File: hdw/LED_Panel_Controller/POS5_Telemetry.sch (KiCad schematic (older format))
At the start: 7 parts

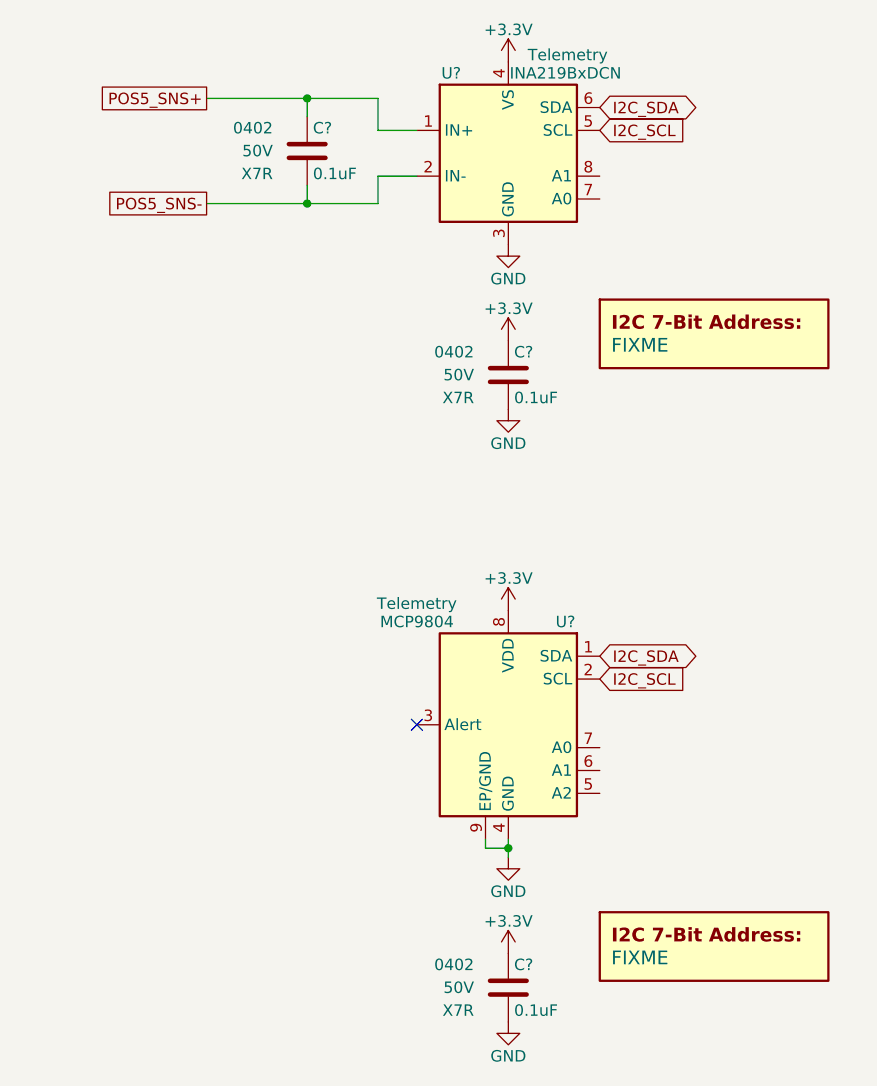
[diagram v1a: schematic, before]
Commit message: fixed level shifter sheet
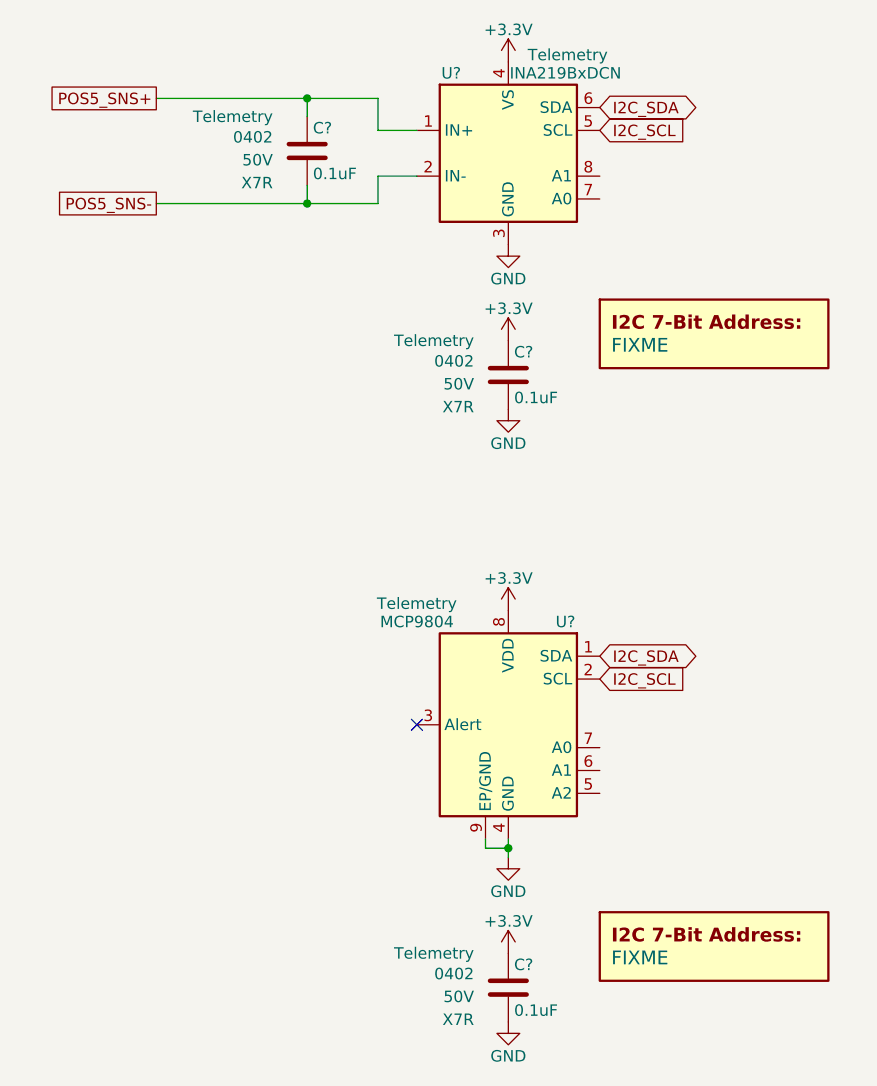
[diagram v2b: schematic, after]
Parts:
- removed C? (x3): 0.1uF, Capacitors_SMD:C_0402, symbol Custom_Library:C_Custom
- added C? (x3): 0.1uF, Capacitors_SMD:C_0402, symbol Custom_Library:C_Custom
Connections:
- net +3V3: now also C?.1, C?.1
- net GND: now also C?.2, C?.2
- net POS5_SNS+: now also C?.1
- net POS5_SNS-: now also C?.2
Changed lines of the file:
@@
 Comment4 ""
 $EndDescr
-Text GLabel 3790 1800 0    50   UnSpc ~ 0
+Text GLabel 3570 1800 0    50   UnSpc ~ 0
 POS5_SNS+
-Text GLabel 3790 2260 0    50   UnSpc ~ 0
+Text GLabel 3570 2260 0    50   UnSpc ~ 0
 POS5_SNS-
 $Comp
@@
 AR Path="/5EAE2D84/5E0ACFF2" Ref="#PWR?"  Part="1"
 AR Path="/5F581B58/5E0ACFF2" Ref="#PWR?"  Part="1"
+AR Path="/5F581B77/5E0ACFF2" Ref="#PWR?"  Part="1"
 AR Path="/5F581BB7/5E0ACFF2" Ref="#PWR?"  Part="1"
 F 0 "#PWR?" H 5110 2190 50  0001 C CNN
@@
 AR Path="/5EAE2D84/5E0AD665" Ref="#PWR?"  Part="1"
 AR Path="/5F581B58/5E0AD665" Ref="#PWR?"  Part="1"
+AR Path="/5F581B77/5E0AD665" Ref="#PWR?"  Part="1"
 AR Path="/5F581BB7/5E0AD665" Ref="#PWR?"  Part="1"
 F 0 "#PWR?" H 5110 1490 50  0001 C CNN
@@
 Text GLabel 5510 1940 2    50   Input ~ 0
 I2C_SCL
-$Comp
-L Custom_Library:C_Custom C?
-U 1 1 5E0B2427
-P 5110 3010
-AR Path="/5B3E071A/5E0B2427" Ref="C?"  Part="1"
-AR Path="/5E0652BA/5E0B2427" Ref="C?"  Part="1"
-AR Path="/5E0A0E29/5E0B2427" Ref="C?"  Part="1"
-AR Path="/5E052856/5E0B2427" Ref="C?"  Part="1"
-AR Path="/5EAE2D84/5E0B2427" Ref="C?"  Part="1"
-AR Path="/5F581B58/5E0B2427" Ref="C?"  Part="1"
-AR Path="/5F581BB7/5E0B2427" Ref="C?"  Part="1"
-F 0 "C?" H 5135 3110 50  0000 L CNN
-F 1 "0.1uF" H 5135 2910 50  0000 L CNN
-F 2 "Capacitors_SMD:C_0402" H 5148 2860 50  0001 C CNN
-F 3 "" H 5135 3110 50  0001 C CNN
-F 4 "0402" H 4960 3110 50  0000 R CNN "display_footprint"
-F 5 "50V" H 4960 3010 50  0000 R CNN "Voltage"
-F 6 "X7R" H 4960 2910 50  0000 R CNN "Dielectric"
-F 7 "" H 1200 -3870 50  0001 C CNN "Digi-Key PN"
-	1    5110 3010
-	1    0    0    -1
-$EndComp
 $Comp
 L power:+3.3V #PWR?
@@
 AR Path="/5EAE2D84/5E0B535B" Ref="#PWR?"  Part="1"
 AR Path="/5F581B58/5E0B535B" Ref="#PWR?"  Part="1"
+AR Path="/5F581B77/5E0B535B" Ref="#PWR?"  Part="1"
 AR Path="/5F581BB7/5E0B535B" Ref="#PWR?"  Part="1"
 F 0 "#PWR?" H 5110 2710 50  0001 C CNN
@@
 AR Path="/5EAE2D84/5E0B592B" Ref="#PWR?"  Part="1"
 AR Path="/5F581B58/5E0B592B" Ref="#PWR?"  Part="1"
+AR Path="/5F581B77/5E0B592B" Ref="#PWR?"  Part="1"
 AR Path="/5F581BB7/5E0B592B" Ref="#PWR?"  Part="1"
 F 0 "#PWR?" H 5110 2910 50  0001 C CNN
@@
 AR Path="/5EAE2D84/5E0B8BC8" Ref="DOC?"  Part="1"
 AR Path="/5F581B58/5E0B8BC8" Ref="DOC?"  Part="1"
+AR Path="/5F581B77/5E0B8BC8" Ref="DOC?"  Part="1"
 AR Path="/5F581BB7/5E0B8BC8" Ref="DOC?"  Part="1"
 F 0 "DOC?" H 6010 3130 60  0001 C CNN
@@
 AR Path="/5EAE2D84/5E2AA995" Ref="#PWR?"  Part="1"
 AR Path="/5F581B58/5E2AA995" Ref="#PWR?"  Part="1"
+AR Path="/5F581B77/5E2AA995" Ref="#PWR?"  Part="1"
 AR Path="/5F581BB7/5E2AA995" Ref="#PWR?"  Part="1"
 F 0 "#PWR?" H 5110 4870 50  0001 C CNN
@@
 AR Path="/5EAE2D84/5E2AA99A" Ref="#PWR?"  Part="1"
 AR Path="/5F581B58/5E2AA99A" Ref="#PWR?"  Part="1"
+AR Path="/5F581B77/5E2AA99A" Ref="#PWR?"  Part="1"
 AR Path="/5F581BB7/5E2AA99A" Ref="#PWR?"  Part="1"
 F 0 "#PWR?" H 5110 3890 50  0001 C CNN
@@
 AR Path="/5EAE2D84/5E2AA99D" Ref="U?"  Part="1"
 AR Path="/5F581B58/5E2AA99D" Ref="U?"  Part="1"
+AR Path="/5F581B77/5E2AA99D" Ref="U?"  Part="1"
 AR Path="/5F581BB7/5E2AA99D" Ref="U?"  Part="1"
 F 0 "U?" H 4860 4990 50  0000 C CNN
@@
 NoConn ~ 4710 4540
 $Comp
-L Custom_Library:C_Custom C?
-U 1 1 5E2AA9A1
-P 5110 5690
-AR Path="/5B3E071A/5E2AA9A1" Ref="C?"  Part="1"
-AR Path="/5E0652BA/5E2AA9A1" Ref="C?"  Part="1"
-AR Path="/5E0A0E29/5E2AA9A1" Ref="C?"  Part="1"
-AR Path="/5E052856/5E2AA9A1" Ref="C?"  Part="1"
-AR Path="/5EAE2D84/5E2AA9A1" Ref="C?"  Part="1"
-AR Path="/5F581B58/5E2AA9A1" Ref="C?"  Part="1"
-AR Path="/5F581BB7/5E2AA9A1" Ref="C?"  Part="1"
-F 0 "C?" H 5135 5790 50  0000 L CNN
-F 1 "0.1uF" H 5135 5590 50  0000 L CNN
-F 2 "Capacitors_SMD:C_0402" H 5148 5540 50  0001 C CNN
-F 3 "" H 5135 5790 50  0001 C CNN
-F 4 "0402" H 4960 5790 50  0000 R CNN "display_footprint"
-F 5 "50V" H 4960 5690 50  0000 R CNN "Voltage"
-F 6 "X7R" H 4960 5590 50  0000 R CNN "Dielectric"
-F 7 "" H 1200 -1190 50  0001 C CNN "Digi-Key PN"
-	1    5110 5690
-	1    0    0    -1
-$EndComp
-$Comp
 L power:+3.3V #PWR?
 U 1 1 5E2AA9A6
@@
 AR Path="/5EAE2D84/5E2AA9A6" Ref="#PWR?"  Part="1"
 AR Path="/5F581B58/5E2AA9A6" Ref="#PWR?"  Part="1"
+AR Path="/5F581B77/5E2AA9A6" Ref="#PWR?"  Part="1"
 AR Path="/5F581BB7/5E2AA9A6" Ref="#PWR?"  Part="1"
 F 0 "#PWR?" H 5110 5390 50  0001 C CNN
@@
 AR Path="/5EAE2D84/5E2AA9AD" Ref="#PWR?"  Part="1"
 AR Path="/5F581B58/5E2AA9AD" Ref="#PWR?"  Part="1"
+AR Path="/5F581B77/5E2AA9AD" Ref="#PWR?"  Part="1"
 AR Path="/5F581BB7/5E2AA9AD" Ref="#PWR?"  Part="1"
 F 0 "#PWR?" H 5110 5590 50  0001 C CNN
@@
 AR Path="/5EAE2D84/5E2AA9AF" Ref="DOC?"  Part="1"
 AR Path="/5F581B58/5E2AA9AF" Ref="DOC?"  Part="1"
+AR Path="/5F581B77/5E2AA9AF" Ref="DOC?"  Part="1"
 AR Path="/5F581BB7/5E2AA9AF" Ref="DOC?"  Part="1"
 F 0 "DOC?" H 6010 5810 60  0001 C CNN
@@
 Wire Wire Line
 	4230 1880 4230 1800
-$Comp
-L Custom_Library:C_Custom C?
-U 1 1 5E07E0FD
-P 4230 2030
-AR Path="/5B3E071A/5E07E0FD" Ref="C?"  Part="1"
-AR Path="/5E0652BA/5E07E0FD" Ref="C?"  Part="1"
-AR Path="/5E0A0E29/5E07E0FD" Ref="C?"  Part="1"
-AR Path="/5E052856/5E07E0FD" Ref="C?"  Part="1"
-AR Path="/5EAE2D84/5E07E0FD" Ref="C?"  Part="1"
-AR Path="/5F581B58/5E07E0FD" Ref="C?"  Part="1"
-AR Path="/5F581BB7/5E07E0FD" Ref="C?"  Part="1"
-F 0 "C?" H 4255 2130 50  0000 L CNN
-F 1 "0.1uF" H 4255 1930 50  0000 L CNN
-F 2 "Capacitors_SMD:C_0402" H 4268 1880 50  0001 C CNN
-F 3 "" H 4255 2130 50  0001 C CNN
-F 4 "0402" H 4080 2130 50  0000 R CNN "display_footprint"
-F 5 "50V" H 4080 2030 50  0000 R CNN "Voltage"
-F 6 "X7R" H 4080 1930 50  0000 R CNN "Dielectric"
-F 7 "" H 320 -4850 50  0001 C CNN "Digi-Key PN"
-	1    4230 2030
-	1    0    0    -1
-$EndComp
-Wire Wire Line
-	3790 2260 4230 2260
-Wire Wire Line
-	3790 1800 4230 1800
 $Comp
 L Analog_ADC:INA219BxDCN U?
@@
 	4540 2260 4230 2260
 Connection ~ 4230 2260
+$Comp
+L Custom_Library:C_Custom C?
+U 1 1 6018BD18
+P 4230 2030
+AR Path="/5B3E071A/6018BD18" Ref="C?"  Part="1"
+AR Path="/5E0652BA/6018BD18" Ref="C?"  Part="1"
+AR Path="/5E0A0E29/6018BD18" Ref="C?"  Part="1"
+AR Path="/5E052856/6018BD18" Ref="C?"  Part="1"
+AR Path="/5EAE2D84/6018BD18" Ref="C?"  Part="1"
+AR Path="/5F581B58/6018BD18" Ref="C?"  Part="1"
+AR Path="/5F581B77/6018BD18" Ref="C?"  Part="1"
+AR Path="/5F581BB7/6018BD18" Ref="C?"  Part="1"
+F 0 "C?" H 4255 2130 50  0000 L CNN
+F 1 "0.1uF" H 4255 1930 50  0000 L CNN
+F 2 "Capacitors_SMD:C_0402" H 4268 1880 50  0001 C CNN
+F 3 "" H 4255 2130 50  0001 C CNN
+F 4 "0402" H 4080 2090 50  0000 R CNN "display_footprint"
+F 5 "50V" H 4080 1990 50  0000 R CNN "Voltage"
+F 6 "X7R" H 4080 1890 50  0000 R CNN "Dielectric"
+F 7 "Telemetry" H 4080 2180 50  0000 R CNN "Configuration"
+	1    4230 2030
+	1    0    0    -1
+$EndComp
+Wire Wire Line
+	3570 1800 4230 1800
+Wire Wire Line
+	3570 2260 4230 2260
+$Comp
+L Custom_Library:C_Custom C?
+U 1 1 6018C640
+P 5110 5690
+AR Path="/5B3E071A/6018C640" Ref="C?"  Part="1"
+AR Path="/5E0652BA/6018C640" Ref="C?"  Part="1"
+AR Path="/5E0A0E29/6018C640" Ref="C?"  Part="1"
+AR Path="/5E052856/6018C640" Ref="C?"  Part="1"
+AR Path="/5EAE2D84/6018C640" Ref="C?"  Part="1"
+AR Path="/5F581B58/6018C640" Ref="C?"  Part="1"
+AR Path="/5F581B77/6018C640" Ref="C?"  Part="1"
+AR Path="/5F581BB7/6018C640" Ref="C?"  Part="1"
+F 0 "C?" H 5135 5790 50  0000 L CNN
+F 1 "0.1uF" H 5135 5590 50  0000 L CNN
+F 2 "Capacitors_SMD:C_0402" H 5148 5540 50  0001 C CNN
+F 3 "" H 5135 5790 50  0001 C CNN
+F 4 "0402" H 4960 5750 50  0000 R CNN "display_footprint"
+F 5 "50V" H 4960 5650 50  0000 R CNN "Voltage"
+F 6 "X7R" H 4960 5550 50  0000 R CNN "Dielectric"
+F 7 "Telemetry" H 4960 5840 50  0000 R CNN "Configuration"
+	1    5110 5690
+	1    0    0    -1
+$EndComp
+$Comp
+L Custom_Library:C_Custom C?
+U 1 1 6018CFFA
+P 5110 3010
+AR Path="/5B3E071A/6018CFFA" Ref="C?"  Part="1"
+AR Path="/5E0652BA/6018CFFA" Ref="C?"  Part="1"
+AR Path="/5E0A0E29/6018CFFA" Ref="C?"  Part="1"
+AR Path="/5E052856/6018CFFA" Ref="C?"  Part="1"
+AR Path="/5EAE2D84/6018CFFA" Ref="C?"  Part="1"
+AR Path="/5F581B58/6018CFFA" Ref="C?"  Part="1"
+AR Path="/5F581B77/6018CFFA" Ref="C?"  Part="1"
+AR Path="/5F581BB7/6018CFFA" Ref="C?"  Part="1"
+F 0 "C?" H 5135 3110 50  0000 L CNN
+F 1 "0.1uF" H 5135 2910 50  0000 L CNN
+F 2 "Capacitors_SMD:C_0402" H 5148 2860 50  0001 C CNN
+F 3 "" H 5135 3110 50  0001 C CNN
+F 4 "0402" H 4960 3070 50  0000 R CNN "display_footprint"
+F 5 "50V" H 4960 2970 50  0000 R CNN "Voltage"
+F 6 "X7R" H 4960 2870 50  0000 R CNN "Dielectric"
+F 7 "Telemetry" H 4960 3160 50  0000 R CNN "Configuration"
+	1    5110 3010
+	1    0    0    -1
+$EndComp
 $EndSCHEMATC

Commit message: added digikey pns, footprints, bom scrubbed
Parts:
- C? (x3): Digi-Key PN (none) -> 490-10701-1-ND
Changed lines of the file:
@@
 F 6 "X7R" H 4080 1890 50  0000 R CNN "Dielectric"
 F 7 "Telemetry" H 4080 2180 50  0000 R CNN "Configuration"
+F 8 "490-10701-1-ND" H 4230 2030 50  0001 C CNN "Digi-Key PN"
 	1    4230 2030
 	1    0    0    -1
@@
 F 6 "X7R" H 4960 5550 50  0000 R CNN "Dielectric"
 F 7 "Telemetry" H 4960 5840 50  0000 R CNN "Configuration"
+F 8 "490-10701-1-ND" H 5110 5690 50  0001 C CNN "Digi-Key PN"
 	1    5110 5690
 	1    0    0    -1
@@
 F 6 "X7R" H 4960 2870 50  0000 R CNN "Dielectric"
 F 7 "Telemetry" H 4960 3160 50  0000 R CNN "Configuration"
+F 8 "490-10701-1-ND" H 5110 3010 50  0001 C CNN "Digi-Key PN"
 	1    5110 3010
 	1    0    0    -1

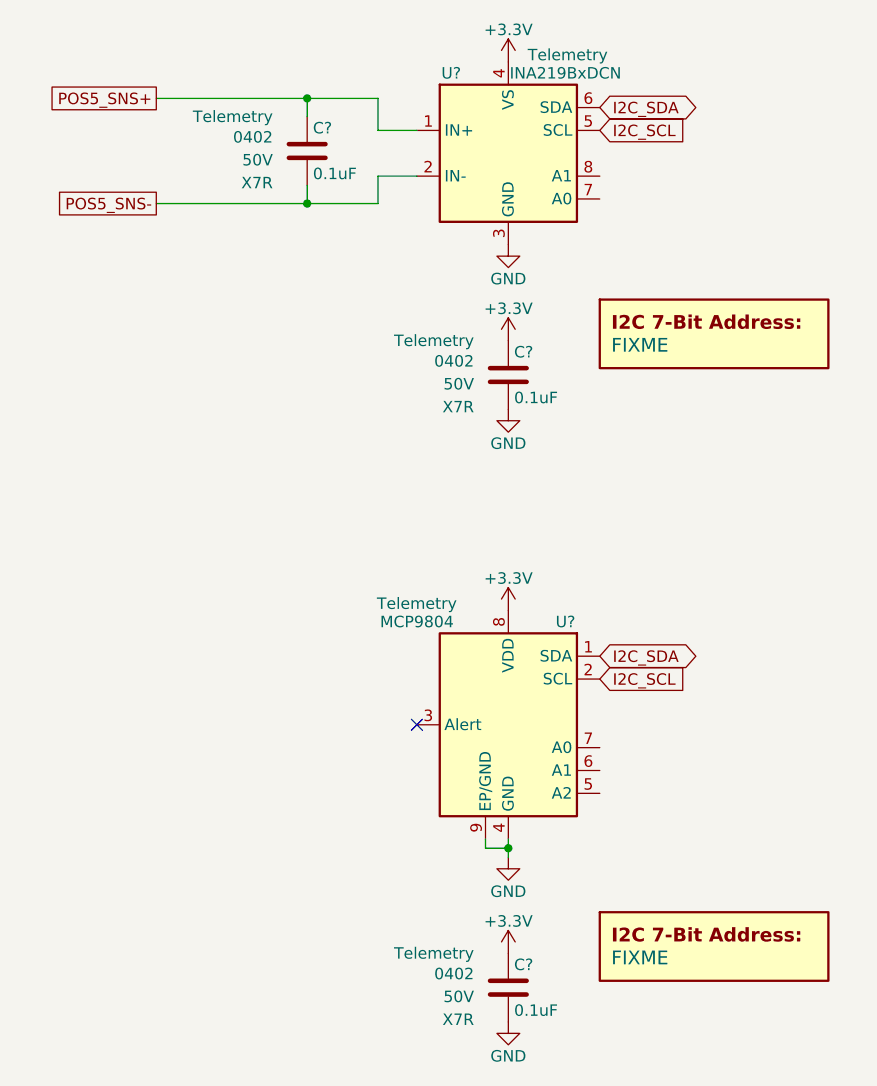
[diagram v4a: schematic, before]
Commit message: assigned I2C addresses
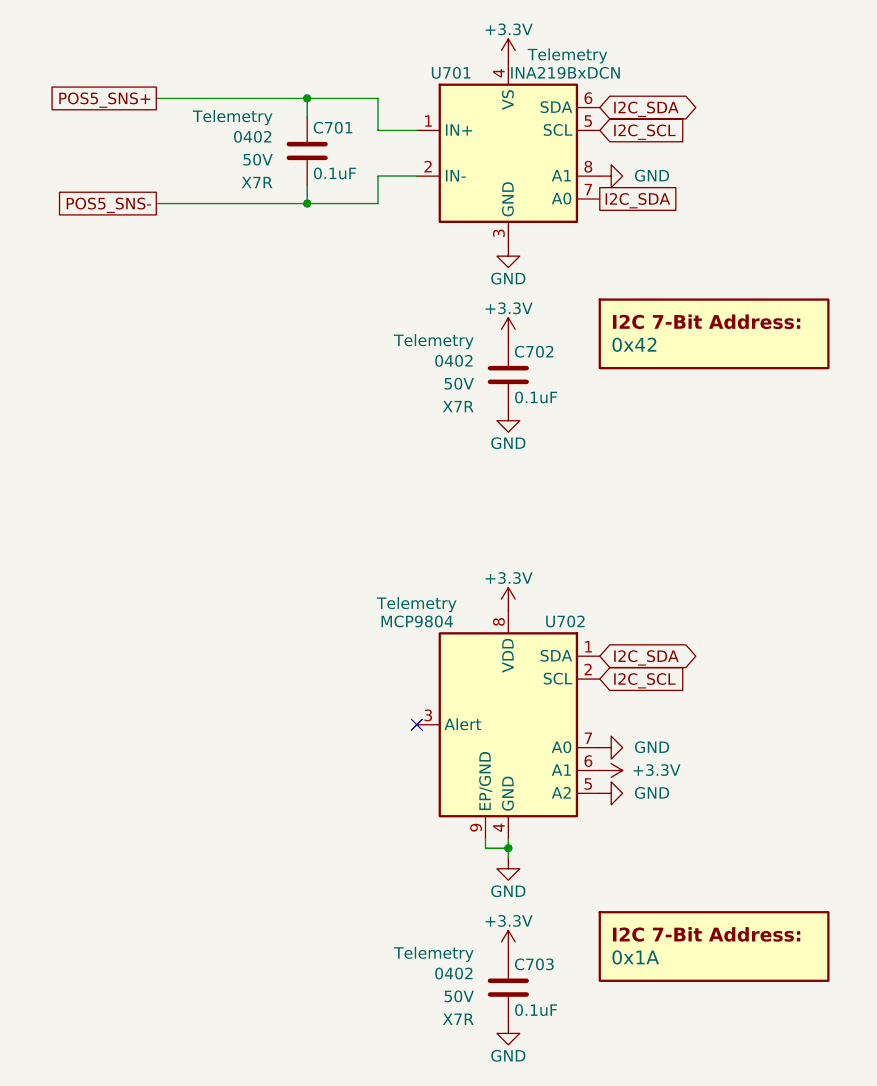
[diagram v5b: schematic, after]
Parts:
- removed C? (x3): 0.1uF, Capacitors_SMD:C_0402, symbol Custom_Library:C_Custom
- removed DOC? (x2): FIXME, symbol Custom_Library:I2C_Address
- removed U?: INA219BxDCN, Package_TO_SOT_SMD:SOT-23-8, symbol Analog_ADC:INA219BxDCN
- removed U?: MCP9804, Package_DFN_QFN:DFN-8-1EP_3x2mm_P0.5mm_EP1.3x1.5mm, symbol Sensor_Temperature:MCP9804_DFN
- added C701, C702, C703: 0.1uF, Capacitors_SMD:C_0402, symbol Custom_Library:C_Custom
- added DOC701: 0x42, symbol Custom_Library:I2C_Address
- added DOC702: 0x1A, symbol Custom_Library:I2C_Address
- added U701: INA219BxDCN, Package_TO_SOT_SMD:SOT-23-8, symbol Analog_ADC:INA219BxDCN
- added U702: MCP9804, Package_DFN_QFN:DFN-8-1EP_3x2mm_P0.5mm_EP1.3x1.5mm, symbol Sensor_Temperature:MCP9804_DFN
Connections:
- net +3V3: now also C702.1, C703.1, U701.4 (VS), U702.6 (A1), U702.8 (VDD)
- net GND: now also C702.2, C703.2, U701.3 (GND), U701.8 (A1), U702.4 (GND), U702.5 (A2), U702.7 (A0), U702.9 (EP/GND)
- net I2C_SCL: now also U701.5 (SCL), U702.2 (SCL)
- net I2C_SDA: now also U701.6 (SDA), U701.7 (A0), U702.1 (SDA)
- net POS5_SNS+: now also C701.1, U701.1 (IN+)
- net POS5_SNS-: now also C701.2, U701.2 (IN-)

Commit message: added BOMs, some consolidation
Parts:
- C701, C702, C703: Digi-Key PN 490-10701-1-ND -> 490-10698-1-ND
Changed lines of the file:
@@
 F 6 "X7R" H 4080 1890 50  0000 R CNN "Dielectric"
 F 7 "Telemetry" H 4080 2180 50  0000 R CNN "Configuration"
-F 8 "490-10701-1-ND" H 4230 2030 50  0001 C CNN "Digi-Key PN"
+F 8 "490-10698-1-ND" H 4230 2030 50  0001 C CNN "Digi-Key PN"
 	1    4230 2030
 	1    0    0    -1
@@
 F 6 "X7R" H 4960 5550 50  0000 R CNN "Dielectric"
 F 7 "Telemetry" H 4960 5840 50  0000 R CNN "Configuration"
-F 8 "490-10701-1-ND" H 5110 5690 50  0001 C CNN "Digi-Key PN"
+F 8 "490-10698-1-ND" H 5110 5690 50  0001 C CNN "Digi-Key PN"
 	1    5110 5690
 	1    0    0    -1
@@
 F 6 "X7R" H 4960 2870 50  0000 R CNN "Dielectric"
 F 7 "Telemetry" H 4960 3160 50  0000 R CNN "Configuration"
-F 8 "490-10701-1-ND" H 5110 3010 50  0001 C CNN "Digi-Key PN"
+F 8 "490-10698-1-ND" H 5110 3010 50  0001 C CNN "Digi-Key PN"
 	1    5110 3010
 	1    0    0    -1
